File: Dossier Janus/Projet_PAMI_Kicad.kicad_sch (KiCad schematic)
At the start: 11 parts, among them J1 Conn_02x07_Odd_Even, SW1 SW_Push, U1 STM32L552CCTx

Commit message: ajout dossier+modif Kicad
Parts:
- added C10, C12, C13, C9: C, symbol Device:C
- added C11: 15.8n, symbol Device:C
- added C14: 8.7n, symbol Device:C
- added D1, D2: D_Schottky, symbol Device:D_Schottky
- added H1, H2, H3, H4: MountingHole_Pad, symbol Mechanical:MountingHole_Pad
- added L1, L2: L, symbol Device:L
- added R1: 240, symbol Device:R
- added R2, R4: 1.2k, symbol Device:R
- added R3: 1.8k, symbol Device:R
- added R5: 1.5k, symbol Device:R
- added R6: 2.2k, symbol Device:R
- added U1, U4: LM2596S-3.3, Package_TO_SOT_SMD:TO-263-5_TabPin3, symbol Regulator_Switching:LM2596S-3.3
- added U3: ~, symbol nucleo-g431kb:Alimentation_Pami
- renumbered C6 to C1, C5 to C2, C4 to C3, C3 to C4, C2 to C5, C8 to C6, C1 to C7, C9 to C8, J1 to ST-LINK1, U1 to U2
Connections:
- net +3.3V: now also ST-LINK1.3 (Pin_3)
- net GND: now also ST-LINK1.11 (Pin_11), ST-LINK1.5 (Pin_5), ST-LINK1.7 (Pin_7), C10.2, C12.2, C13.2, C9.2, D1.2 (A), D2.2 (A), H1.1, H2.1, H3.1, H4.1, R2.1, R4.1, U1.3 (GND), U1.5 (~{ON}/OFF), U3. (GND), U4.3 (GND), U4.5 (~{ON}/OFF)
- net STLINK_RX: now reaches ST-LINK1.13 (Pin_13)
- net STLINK_TX: now reaches ST-LINK1.14 (Pin_14)
- net SWDIO: now reaches ST-LINK1.4 (Pin_4)
- net SWCLK: now reaches ST-LINK1.6 (Pin_6)
- new net: C13.1, C14.2, L2.2, R6.2
- new net: D2.1 (K), L2.1, U4.2 (OUT)
- new net: C14.1, R4.2, R5.1, U4.4 (FB)
- new net: D1.1 (K), L1.1, U1.2 (OUT)
- new net: C10.1, C11.2, L1.2, R1.2
- new net: C11.1, R2.2, R3.1, U1.4 (FB)
- new net: R1.1, R3.2
- new net: R5.2, R6.1
- new net +7.5V: C12.1, C9.1, U1.1 (VIN), U4.1 (VIN)
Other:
- note added: "Trous de fixation"
- moved on the sheet: ST-LINK1

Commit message: Finalisation schematic + ressources
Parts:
- removed C10, C12, C9: C, symbol Device:C
- removed C11: 15.8n, symbol Device:C
- removed C14: 8.7n, symbol Device:C
- removed D1, D2: D_Schottky, symbol Device:D_Schottky
- removed L1, L2: L, symbol Device:L
- removed R1: 240, symbol Device:R
- removed R2, R4: 1.2k, symbol Device:R
- removed R3: 1.8k, symbol Device:R
- removed R5: 1.5k, symbol Device:R
- removed R6: 2.2k, symbol Device:R
- removed ST-LINK1: Conn_02x07_Odd_Even, symbol Connector_Generic:Conn_02x07_Odd_Even
- removed SW1: SW_Push, symbol Switch:SW_Push
- removed U1, U4: LM2596S-3.3, Package_TO_SOT_SMD:TO-263-5_TabPin3, symbol Regulator_Switching:LM2596S-3.3
- added 39n1: WE-LQS_8040, WE-LQS_8040:WE-LQS_8040, symbol WE-LQS_8040:WE-LQS_8040
- added C1, C14, C15, C3: 10u, Capacitor_SMD:C_Elec_4x5.4, symbol Device:C_Polarized
- added C17: 100n, Capacitor_SMD:C_0402_1005Metric_Pad0.74x0.62mm_HandSolder, symbol Device:C
- added C2, C4: 22u, Capacitor_SMD:C_Elec_5x5.4, symbol Device:C_Polarized
- added J1: FTSH-107-01-F-DV-K, FTSH-107-01-F-DV-K:SAMTEC_FTSH-107-01-F-DV-K, symbol FTSH-107-01-F-DV-K:FTSH-107-01-F-DV-K
- added S1: 430471025826, boutonSMD_wurth430471025826:430471025826, symbol boutonSMD_wurth430471025826:430471025826
- added TP1, TP2: TestPoint, TestPoint:TestPoint_Pad_D2.0mm, symbol Connector:TestPoint
- added U1, U3: ~, Connector_PinHeader_2.54mm:PinHeader_1x03_P2.54mm_Vertical, symbol Library_PAMI:Servo_moteur
- added U10: ~, Connector_PinHeader_2.54mm:PinHeader_1x04_P2.54mm_Vertical, symbol Library_PAMI:Module_Uson
- added U2: ~, Connector_PinHeader_2.54mm:PinHeader_1x06_P2.54mm_Vertical, symbol Library_PAMI:IR_Module_4way
- added U4: AZ1117-5.0, Package_TO_SOT_SMD:SOT-223-3_TabPin2, symbol Regulator_Linear:AZ1117-3.3
- added U5, U6: ~, Connector_PinHeader_2.54mm:PinHeader_1x02_P2.54mm_Vertical, symbol Library_PAMI:Moteur_DC
- added U7: AZ1117-3.3, Package_TO_SOT_SMD:SOT-223-3_TabPin2, symbol Regulator_Linear:AZ1117-3.3
- added U9: TB6612FNG, Package_SO:SSOP-24_5.3x8.2mm_P0.65mm, symbol Driver_Motor:TB6612FNG
- C10: renamed from C6; footprint (none) -> Capacitor_SMD:C_0402_1005Metric_Pad0.74x0.62mm_HandSolder
- C11: renamed from C8; footprint (none) -> Capacitor_SMD:C_0402_1005Metric_Pad0.74x0.62mm_HandSolder
- C12: renamed from C7; value 100n -> 10n; footprint (none) -> Capacitor_SMD:C_0402_1005Metric_Pad0.74x0.62mm_HandSolder
- C13: value C -> 100n; footprint (none) -> Capacitor_SMD:C_0402_1005Metric_Pad0.74x0.62mm_HandSolder
- C5: renamed from C1; footprint (none) -> Capacitor_SMD:C_0805_2012Metric_Pad1.18x1.45mm_HandSolder
- C6: renamed from C2; footprint (none) -> Capacitor_SMD:C_0402_1005Metric_Pad0.74x0.62mm_HandSolder
- C7: renamed from C3; footprint (none) -> Capacitor_SMD:C_0402_1005Metric_Pad0.74x0.62mm_HandSolder
- C8: renamed from C4; footprint (none) -> Capacitor_SMD:C_0402_1005Metric_Pad0.74x0.62mm_HandSolder
- C9: renamed from C5; footprint (none) -> Capacitor_SMD:C_0402_1005Metric_Pad0.74x0.62mm_HandSolder
- H1, H2, H3, H4: footprint (none) -> MountingHole:MountingHole_2.7mm_M2.5_Pad
- U8: renamed from U3; footprint (none) -> Connector_PinHeader_2.54mm:PinHeader_1x02_P2.54mm_Vertical
- renumbered U2 to U11
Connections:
- net +3.3V: now also 39n1.2, C15.1, C17.1, C4.1, J1.03, TP2.1, U7.2 (VO), U9.20 (VCC); no longer C10.1, C11.1, U11.9 (VDDA)
- net +7.5V: now also C13.1, C1.1, C14.1, U4.3 (VI), U9.13 (VM2), U9.14 (VM3), U9.24 (VM1)
- net GND: now also C1.2, C14.2, C15.2, C17.2, C2.2, C3.2, C4.2, J1.05, J1.07, J1.11, S1.1, U1. (VCC), U10. (Vcc), U2. (X4), U3. (VCC), U4.1 (GND), U7.1 (GND), U9.10 (PGND2), U9.18 (GND), U9.3 (PGND1), U9.4 (PGND1), U9.9 (PGND2)
- net NRST: now also J1.12, S1.3
- net STLINK_RX: now also U11.13 (PA3), J1.13
- net STLINK_TX: now also U11.12 (PA2), J1.14
- net SWCLK: now also U11.37 (PA14), J1.06
- net SWDIO: now also U11.34 (PA13), J1.04
- net IR_1: now reaches U11.14 (PA4)
- net IR_1: now also U2. (X4)
- net IR_2: now reaches U11.15 (PA5)
- net IR_2: now also U2. (X4)
- net IR_3: now reaches U11.16 (PA6)
- net IR_3: now also U2. (X4)
- net IR_4: now reaches U11.17 (PA7)
- net IR_4: now also U2. (X4)
- net Echo: now reaches U11.18 (PB0)
- net Echo: now also U10. (Vcc)
- net Trig: now reaches U11.19 (PB1)
- net Trig: now also U10. (Vcc)
- net PWMA: now reaches U11.29 (PA8)
- net PWMA: now also U9.23 (PWMA)
- net PWMB: now reaches U11.30 (PA9)
- net PWMB: now also U9.15 (PWMB)
- net STBY: now reaches U11.31 (PA10)
- net STBY: now also U9.19 (STBY)
- net PWM_Servo1: now reaches U11.40 (PB4)
- net PWM_Servo1: now also U1. (VCC)
- net PWM_Servo2: now reaches U11.41 (PB5)
- net PWM_Servo2: now also U3. (VCC)
- net AIN1: now reaches U11.42 (PB6)
- net AIN1: now also U9.21 (AIN1)
- net AIN2: now reaches U11.43 (PB7)
- net AIN2: now also U9.22 (AIN2)
- net BIN1: now reaches U11.45 (PB8)
- net BIN1: now also U9.17 (BIN1)
- net BIN2: now reaches U11.46 (PB9)
- net BIN2: now also U9.16 (BIN2)
- new net +3.3VA: 39n1.1, C10.1, C11.1, U11.9 (VDDA)
- new net +5V: C2.1, C3.1, TP1.1, U1. (VCC), U10. (Vcc), U2. (X4), U3. (VCC), U4.2 (VO), U7.3 (VI)
- new net AO1: U5. (I2), U9.1 (AO1), U9.2 (AO1)
- new net AO2: U5. (I2), U9.5 (AO2), U9.6 (AO2)
- new net BO1: U6. (I2), U9.11 (BO1), U9.12 (BO1)
- new net BO2: U6. (I2), U9.7 (BO2), U9.8 (BO2)
- no-connect marks 8 -> 26
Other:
- note added: "Alimentation des piles et régulateurs de tension"
- note added: "DC Motor"
- note added: "MCU"
- note added: "Module IR 4 voies"
- note added: "Module U-Son"
- note added: "Motor Driver"
- note added: "ST-LINK"
- note added: "Servos"
- moved on the sheet: C10, C11, C12, C5, C6, C7, C8, C9, H1, U11

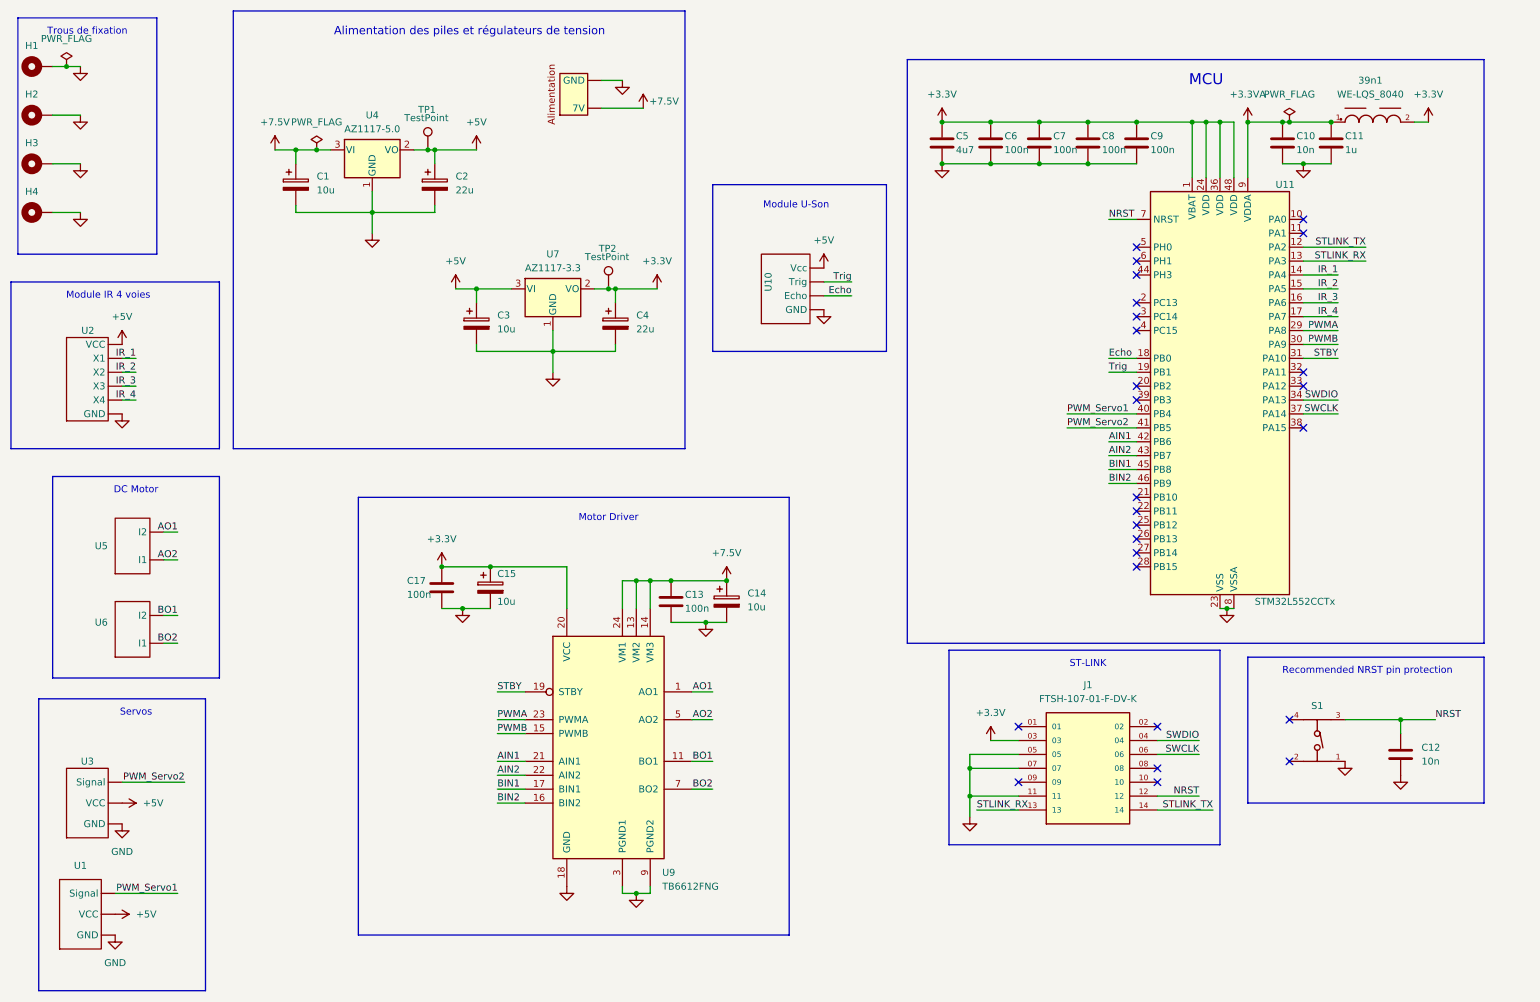
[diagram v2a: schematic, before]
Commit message: correction des oublies de numérotation de pins
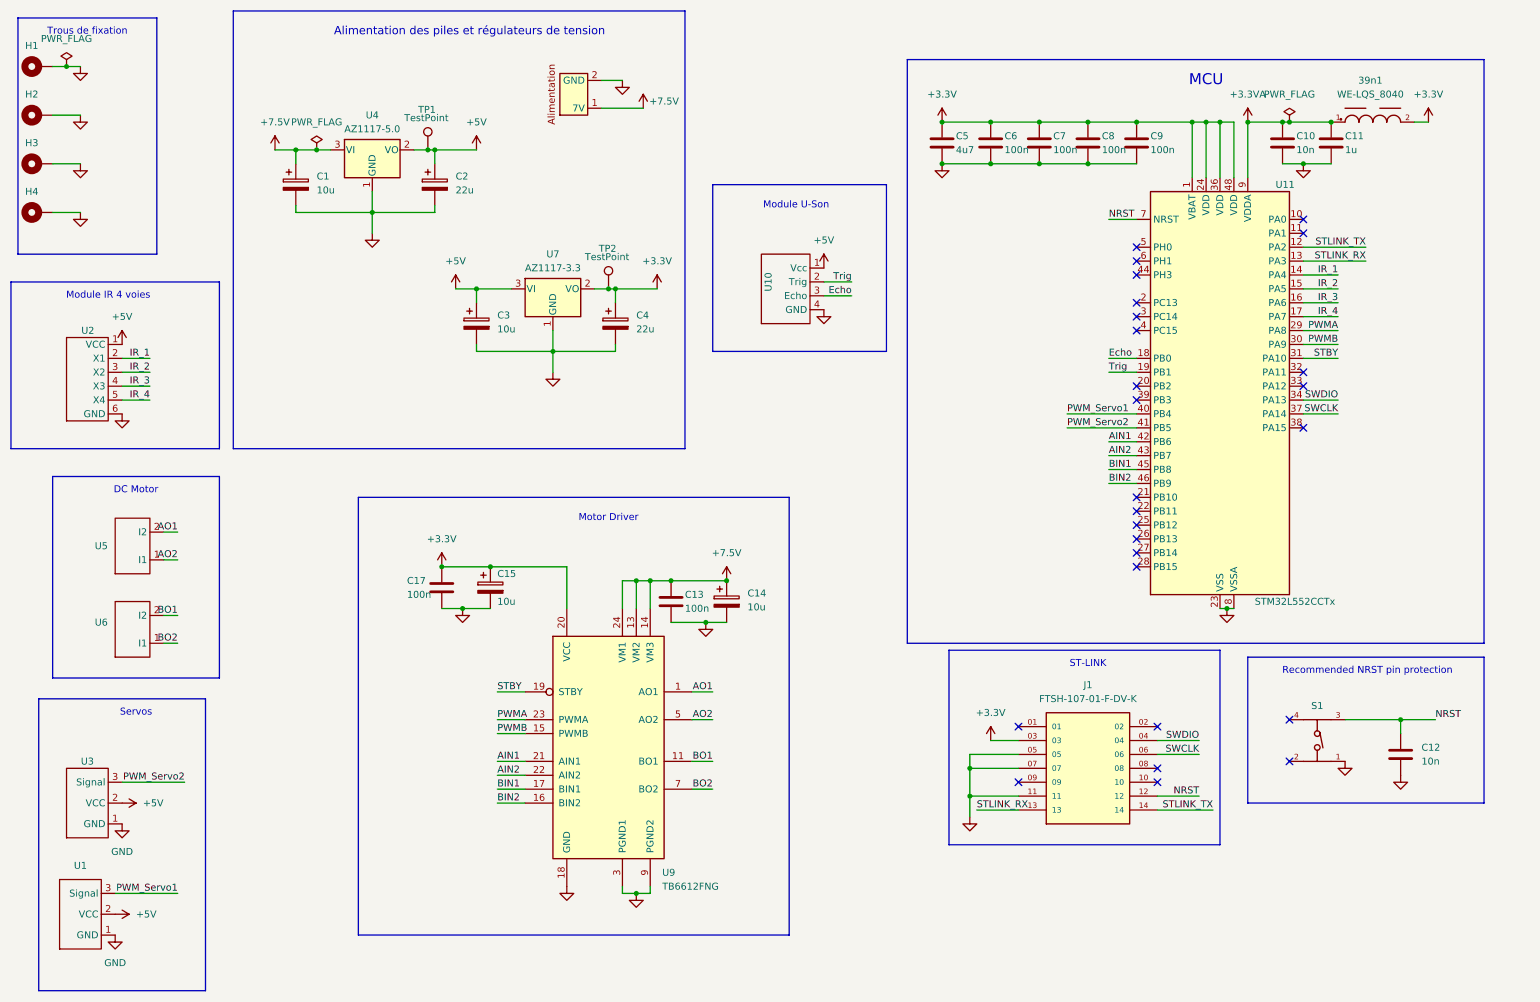
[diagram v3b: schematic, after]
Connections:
- net +5V: now also U1.2 (VCC), U10.1 (Vcc), U2.1 (VCC), U3.2 (VCC); no longer U1. (VCC), U10. (Vcc), U2. (X4), U3. (VCC)
- net AO1: now also U5.2 (I2); no longer U5. (I2)
- net AO2: now also U5.1 (I1); no longer U5. (I2)
- net BO1: now also U6.2 (I2); no longer U6. (I2)
- net BO2: now also U6.1 (I1); no longer U6. (I2)
- net Echo: now also U10.3 (Echo); no longer U10. (Vcc)
- net GND: now also U1.1 (GND), U10.4 (GND), U2.6 (GND), U3.1 (GND), U8.2 (GND); no longer U1. (VCC), U10. (Vcc), U2. (X4), U3. (VCC), U8. (GND)
- net IR_1: now also U2.2 (X1); no longer U2. (X4)
- net IR_2: now also U2.3 (X2); no longer U2. (X4)
- net IR_3: now also U2.4 (X3); no longer U2. (X4)
- net IR_4: now also U2.5 (X4); no longer U2. (X4)
- net PWM_Servo1: now also U1.3 (Signal); no longer U1. (VCC)
- net PWM_Servo2: now also U3.3 (Signal); no longer U3. (VCC)
- net Trig: now also U10.2 (Trig); no longer U10. (Vcc)
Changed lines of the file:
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@@
 	(wire
 		(pts
-			(xy 36.83 83.82) (xy 34.29 83.82)
+			(xy 39.37 83.82) (xy 34.29 83.82)
 		)
 		(stroke
@@
 	(wire
 		(pts
-			(xy 36.83 78.74) (xy 34.29 78.74)
+			(xy 39.37 78.74) (xy 34.29 78.74)
 		)
 		(stroke
@@
 	(wire
 		(pts
-			(xy 36.83 81.28) (xy 34.29 81.28)
+			(xy 39.37 81.28) (xy 34.29 81.28)
 		)
 		(stroke
@@
 	(wire
 		(pts
-			(xy 36.83 76.2) (xy 34.29 76.2)
+			(xy 39.37 76.2) (xy 34.29 76.2)
 		)
 		(stroke
@@
 	)
 	(label "IR_2"
-		(at 36.83 78.74 180)
+		(at 39.37 78.74 180)
 		(effects
 			(font
@@
 	)
 	(label "IR_4"
-		(at 36.83 83.82 180)
+		(at 39.37 83.82 180)
 		(effects
 			(font
@@
 	)
 	(label "IR_1"
-		(at 36.83 76.2 180)
+		(at 39.37 76.2 180)
 		(effects
 			(font
@@
 	)
 	(label "IR_3"
-		(at 36.83 81.28 180)
+		(at 39.37 81.28 180)
 		(effects
 			(font
@@
 			)
 		)
-		(pin ""
+		(pin "3"
 		)
-		(pin ""
+		(pin "1"
 		)
-		(pin ""
+		(pin "6"
 		)
-		(pin ""
+		(pin "5"
 		)
-		(pin ""
+		(pin "4"
 		)
-		(pin ""
+		(pin "2"
 		)
 		(instances
@@
 			)
 		)
-		(pin ""
+		(pin "2"
 		)
-		(pin ""
+		(pin "1"
 		)
 		(instances
@@
 	)
 	(symbol
+		(lib_name "Servo_moteur_1")
 		(lib_id "Library_PAMI:Servo_moteur")
 		(at 27.94 157.48 90)
@@
 			)
 		)
-		(pin ""
+		(pin "1"
 		)
-		(pin ""
+		(pin "3"
 		)
-		(pin ""
+		(pin "2"
 		)
 		(instances
@@
 			)
 		)
-		(pin ""
+		(pin "2"
 		)
-		(pin ""
+		(pin "1"
 		)
 		(instances
@@
 			)
 		)
-		(pin ""
+		(pin "1"
 		)
-		(pin ""
+		(pin "3"
 		)
-		(pin ""
+		(pin "4"
 		)
-		(pin ""
+		(pin "2"
 		)
 		(instances
@@
 	)
 	(symbol
+		(lib_name "Moteur_DC_1")
 		(lib_id "Library_PAMI:Moteur_DC")
 		(at 35.56 110.49 90)
@@
 			)
 		)
-		(pin ""
+		(pin "1"
 		)
-		(pin ""
+		(pin "2"
 		)
 		(instances
@@
 			)
 		)
-		(pin ""
+		(pin "3"
 		)
-		(pin ""
+		(pin "2"
 		)
-		(pin ""
+		(pin "1"
 		)
 		(instances

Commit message: Finalisation PCB
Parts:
- removed 39n1: WE-LQS_8040, WE-LQS_8040:WE-LQS_8040, symbol WE-LQS_8040:WE-LQS_8040
- removed C1, C14, C15, C3: 10u, Capacitor_SMD:C_Elec_4x5.4, symbol Device:C_Polarized
- removed C2, C4: 22u, Capacitor_SMD:C_Elec_5x5.4, symbol Device:C_Polarized
- added C1, C14, C15, C3: 10u, Capacitor_SMD:C_0805_2012Metric, symbol Device:C
- added C2, C4: 22u, Capacitor_SMD:C_0805_2012Metric, symbol Device:C
- added L1: 39n, Inductor_SMD:L_0603_1608Metric, symbol Device:L
- C10, C11, C12, C13, C17, C6, C7, C8, C9: footprint Capacitor_SMD:C_0402_1005Metric_Pad0.74x0.62mm_HandSolder -> Capacitor_SMD:C_0402_1005Metric
- C5: footprint Capacitor_SMD:C_0805_2012Metric_Pad1.18x1.45mm_HandSolder -> Capacitor_SMD:C_0805_2012Metric
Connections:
- net +3.3V: now also C15.1, C4.1, L1.2
- net +3.3VA: now also L1.1
- net +5V: now also C2.1, C3.1
- net +7.5V: now also U8.1 (7V), C1.1, C14.1
- net GND: now also C1.2, C14.2, C15.2, C2.2, C3.2, C4.2
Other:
- moved on the sheet: TP1, U4

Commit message: Rectification
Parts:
- removed C1: 10u, Capacitor_SMD:C_0805_2012Metric, symbol Device:C
- removed C2: 22u, Capacitor_SMD:C_0805_2012Metric, symbol Device:C
- removed U4: AZ1117-5.0, Package_TO_SOT_SMD:SOT-223-3_TabPin2, symbol Regulator_Linear:AZ1117-3.3
- added U12: R-78B5.0-2.0, Converter_DCDC:Converter_DCDC_RECOM_R-78B-2.0_THT, symbol Regulator_Switching:R-78B5.0-2.0
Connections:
- net +5V: now also U12.3 (OUT)
- net +7.5V: now also U12.1 (IN)
- net GND: now also U12.2 (GND)
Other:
- moved on the sheet: TP1

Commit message: Finalisation du PCB--Dossier Janus
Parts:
- IR1: renamed from U2; footprint Connector_PinHeader_2.54mm:PinHeader_1x06_P2.54mm_Vertical -> Connector_JST:JST_XH_S6B-XH-A-1_1x06_P2.50mm_Horizontal
- Moteur1: renamed from U5; footprint Connector_PinHeader_2.54mm:PinHeader_1x02_P2.54mm_Vertical -> Connector_JST:JST_XH_B2B-XH-A_1x02_P2.50mm_Vertical
- Moteur2: renamed from U6; footprint Connector_PinHeader_2.54mm:PinHeader_1x02_P2.54mm_Vertical -> Connector_JST:JST_XH_B2B-XH-A_1x02_P2.50mm_Vertical
- Servo1: renamed from U1; footprint Connector_PinHeader_2.54mm:PinHeader_1x03_P2.54mm_Vertical -> Connector_JST:JST_PH_B3B-PH-K_1x03_P2.00mm_Vertical
- Servo2: renamed from U3; footprint Connector_PinHeader_2.54mm:PinHeader_1x03_P2.54mm_Vertical -> Connector_JST:JST_PH_B3B-PH-K_1x03_P2.00mm_Vertical
- U1: renamed from U8; footprint Connector_PinHeader_2.54mm:PinHeader_1x02_P2.54mm_Vertical -> Connector_JST:JST_PH_B2B-PH-K_1x02_P2.00mm_Vertical
- U2: renamed from U11; value STM32L552CCTx -> MCU
- Uson1: renamed from U10; footprint Connector_PinHeader_2.54mm:PinHeader_1x04_P2.54mm_Vertical -> Connector_JST:JST_PH_B4B-PH-K_1x04_P2.00mm_Vertical
- renumbered C17 to C1, C8 to C10, C9 to C11, C10 to C12, C11 to C13, C12 to C14, C3 to C2, C15 to C3, C13 to C5, C14 to C6, C5 to C7, C6 to C8, C7 to C9, U9 to Driver1, U7 to Regu5v-3v1, U12 to Regu7v-5v1, J1 to ST-LINK1, S1 to Switch1
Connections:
- net PWM_Servo1: now also U2.22 (PB11); no longer U2.40 (PB4)

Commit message: Mise à jour couche d'alimentation
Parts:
- removed H4: MountingHole_Pad, MountingHole:MountingHole_2.7mm_M2.5_Pad, symbol Mechanical:MountingHole_Pad
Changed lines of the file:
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@@
 	(wire
 		(pts
-			(xy 21.59 49.53) (xy 26.67 49.53)
-		)
-		(stroke
-			(width 0)
-			(type default)
-		)
-	)
-	(wire
-		(pts
 			(xy 184.15 33.02) (xy 193.04 33.02)
 		)
@@
 	(rectangle
 		(start 15.24 13.97)
-		(end 40.64 57.15)
+		(end 40.64 46.99)
 		(stroke
 			(width 0)
@@
 	(symbol
 		(lib_id "power:GND")
-		(at 26.67 49.53 0)
-		(unit 1)
-		(exclude_from_sim no)
-		(in_bom yes)
-		(on_board yes)
-		(dnp no)
-		(fields_autoplaced yes)
-		(property "Reference" "#PWR04"
-			(at 26.67 55.88 0)
-			(effects
-				(font
-					(size 1.27 1.27)
-				)
-				(hide yes)
-			)
-		)
-		(property "Value" "GND"
-			(at 26.67 54.61 0)
-			(effects
-				(font
-					(size 1.27 1.27)
-				)
-				(hide yes)
-			)
-		)
-		(property "Footprint" ""
-			(at 26.67 49.53 0)
-			(effects
-				(font
-					(size 1.27 1.27)
-				)
-				(hide yes)
-			)
-		)
-		(property "Datasheet" ""
-			(at 26.67 49.53 0)
-			(effects
-				(font
-					(size 1.27 1.27)
-				)
-				(hide yes)
-			)
-		)
-		(property "Description" "Power symbol creates a global label with name \"GND\" , ground"
-			(at 26.67 49.53 0)
-			(effects
-				(font
-					(size 1.27 1.27)
-				)
-				(hide yes)
-			)
-		)
-		(pin "1"
-		)
-		(instances
-			(project "Projet_PAMI_Kicad"
-				(path "/0499dc40-69b9-42f2-bab0-5a104053ae00"
-					(reference "#PWR04")
-					(unit 1)
-				)
-			)
-		)
-	)
-	(symbol
-		(lib_id "power:GND")
 		(at 250.19 40.64 0)
 		(unit 1)
@@
 					(unit 1)
 				)
-			)
-		)
-	)
-	(symbol
-		(lib_name "MountingHole_Pad_2")
-		(lib_id "Mechanical:MountingHole_Pad")
-		(at 19.05 49.53 90)
-		(unit 1)
-		(exclude_from_sim yes)
-		(in_bom no)
-		(on_board yes)
-		(dnp no)
-		(fields_autoplaced yes)
-		(property "Reference" "H4"
-			(at 17.78 45.72 90)
-			(effects
-				(font
-					(size 1.27 1.27)
-				)
-			)
-		)
-		(property "Value" "MountingHole_Pad"
-			(at 19.0499 46.99 0)
-			(effects
-				(font
-					(size 1.27 1.27)
-				)
-				(justify left)
-				(hide yes)
-			)
-		)
-		(property "Footprint" "MountingHole:MountingHole_2.7mm_M2.5_Pad"
-			(at 19.05 49.53 0)
-			(effects
-				(font
-					(size 1.27 1.27)
-				)
-				(hide yes)
-			)
-		)
-		(property "Datasheet" "~"
-			(at 19.05 49.53 0)
-			(effects
-				(font
-					(size 1.27 1.27)
-				)
-				(hide yes)
-			)
-		)
-		(property "Description" "Mounting Hole with connection"
-			(at 19.05 49.53 0)
-			(effects
-				(font
-					(size 1.27 1.27)
-				)
-				(hide yes)
-			)
-		)
-		(pin "1"
-		)
-		(instances
-			(project "Projet_PAMI_Kicad"
-				(path "/0499dc40-69b9-42f2-bab0-5a104053ae00"
-					(reference "H4")
-					(unit 1)
-				)
